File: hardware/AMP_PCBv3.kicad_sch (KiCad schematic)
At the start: 50 parts, among them CN10 Male_R2, CN7 Male_L1, J1 Input_PWR, J3 LED_Header, J4 VESC_PPM, J5 VESC_COMM, J6 STEERING, M2 Fan_PC_3pin, M3 Fan_PC_3pin, M4 Fan_PC_3pin, M5 Fan_PC_3pin, Q1 DMN2310U, Q2 DMN2310U, Q3 DMN2310U, Q4 DMN2310U, U1 TPS56624x, U2 RFM95W-915S2

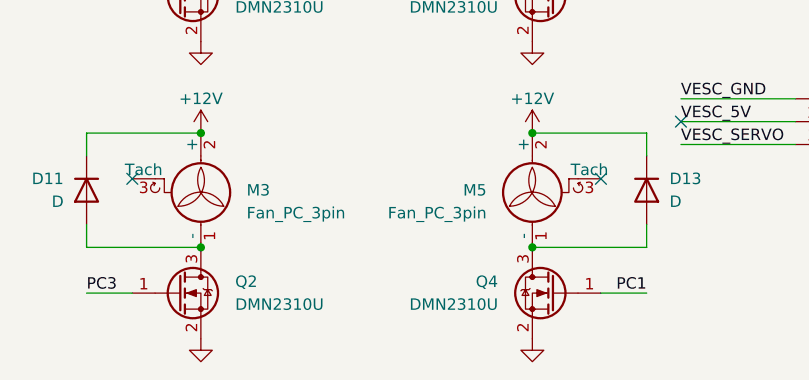
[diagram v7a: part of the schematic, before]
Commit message: Resize board and begin new layout
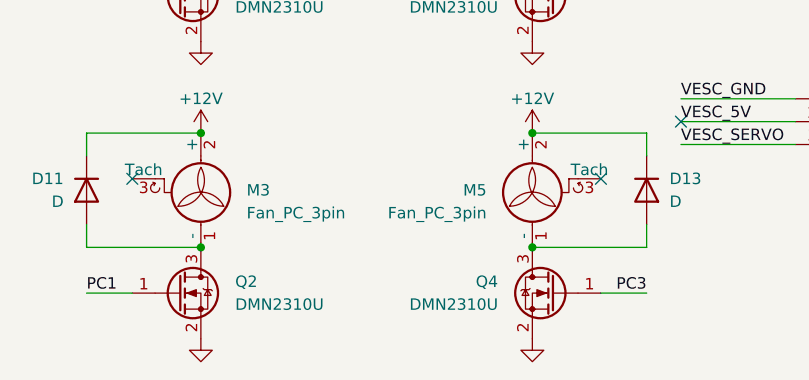
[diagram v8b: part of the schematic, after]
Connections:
- net PC1: now also Q2.1 (G); no longer Q4.1 (G)
- net PC3: now also Q4.1 (G); no longer Q2.1 (G)
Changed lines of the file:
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@@
 	)
 	(label "PC3"
-		(at 25.4 198.12 0)
-		(fields_autoplaced yes)
-		(effects
-			(font
-				(size 1.27 1.27)
-			)
-			(justify left bottom)
+		(at 87.63 198.12 180)
+		(fields_autoplaced yes)
+		(effects
+			(font
+				(size 1.27 1.27)
+			)
+			(justify right bottom)
 		)
 	)
@@
 	)
 	(label "PC1"
-		(at 87.63 198.12 180)
-		(fields_autoplaced yes)
-		(effects
-			(font
-				(size 1.27 1.27)
-			)
-			(justify right bottom)
-		)
-	)
+		(at 25.4 198.12 0)
+		(fields_autoplaced yes)
+		(effects
+			(font
+				(size 1.27 1.27)
+			)
+			(justify left bottom)
+		)
+	)
